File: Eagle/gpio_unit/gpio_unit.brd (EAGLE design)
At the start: 90.5 x 25.4 mm, 11 parts, among them X1 RASPI_GPIO_B+_PIN

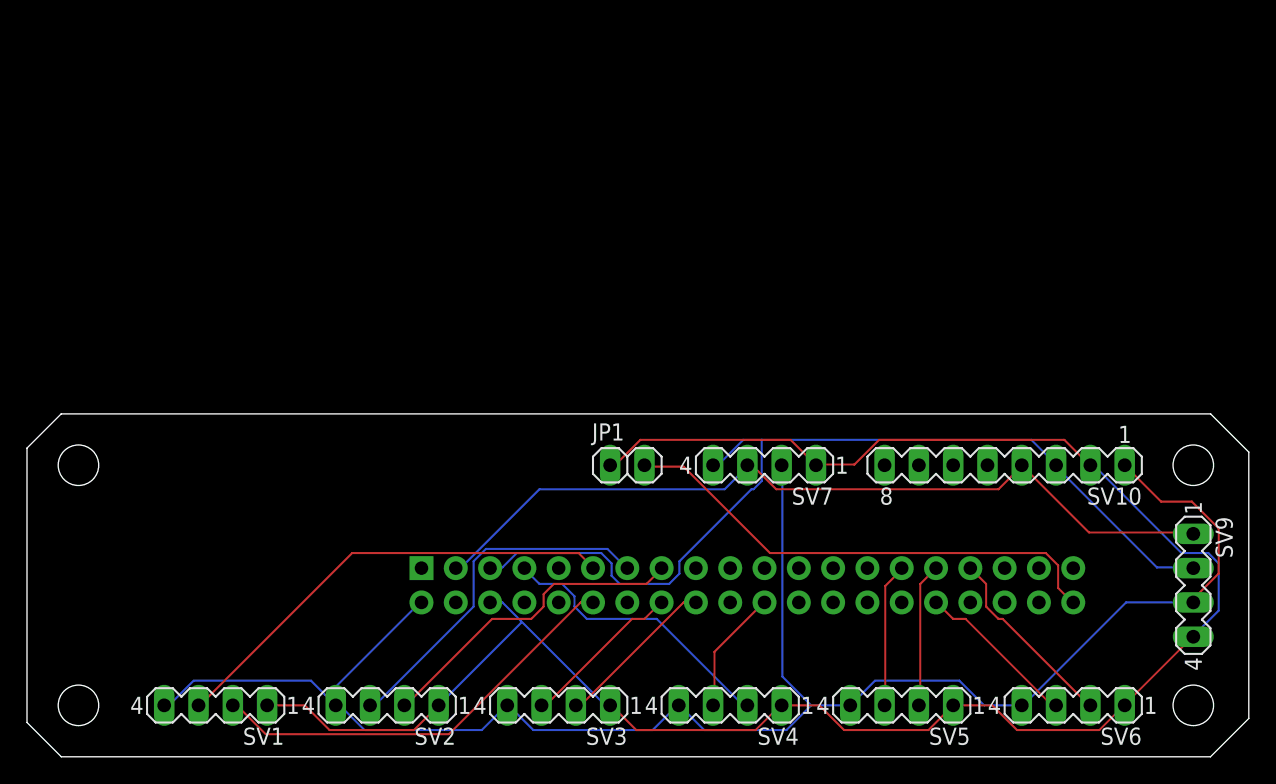
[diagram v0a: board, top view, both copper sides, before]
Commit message: RPi GPIO unit
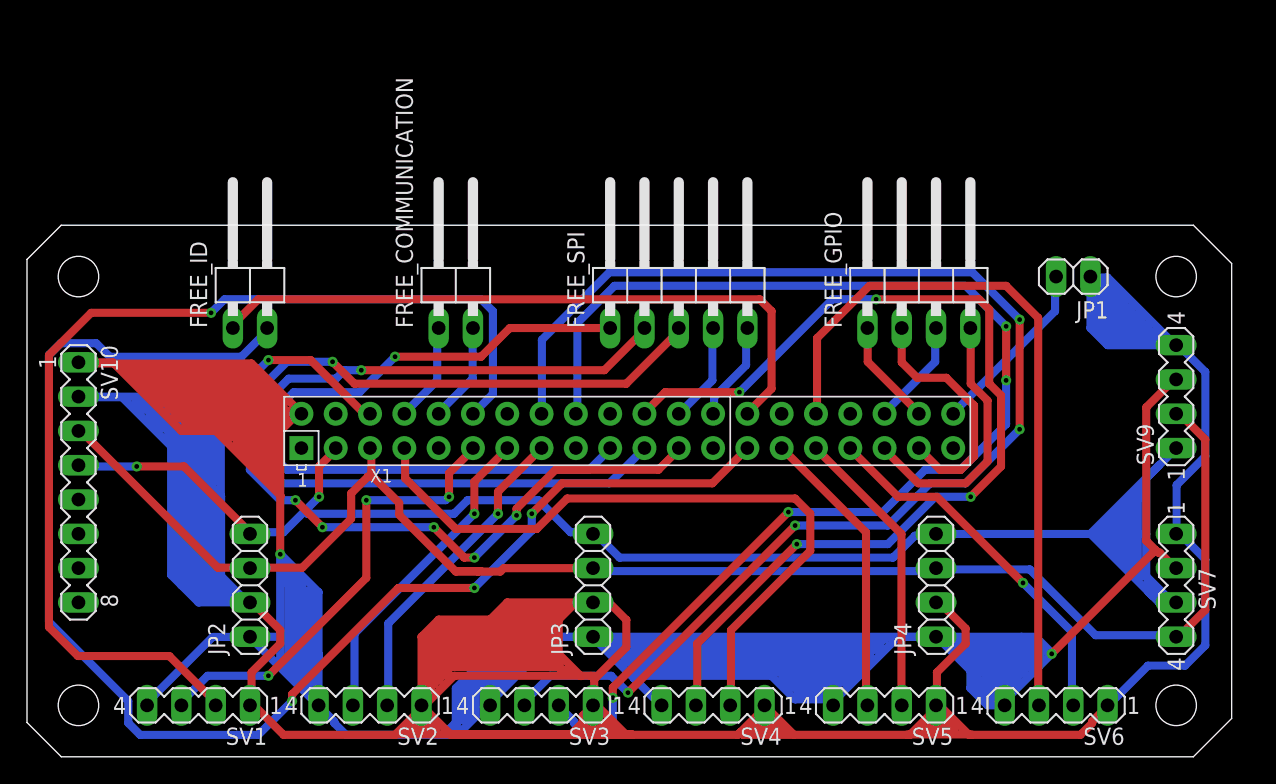
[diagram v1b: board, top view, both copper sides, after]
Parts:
- added FREE_COMMUNICATION, FREE_ID: (no value), pinhead:1X02/90
- added FREE_GPIO: (no value), pinhead:1X04/90
- added FREE_SPI: (no value), pinhead:1X05/90
- added JP2, JP3, JP4: (no value), pinhead:1X04
- moved SV10 68.6 mm to (3.81, 20.3), turned to 270 degrees
- moved JP1 35.9 mm to (77.5, 35.6), turned to 180 degrees
- moved SV7 31.8 mm to (85.1, 12.7), turned to 270 degrees
- moved X1 14.5 mm to (44.5, 24.1), flipped to the top, turned to 0 degrees
- moved SV9 14.0 mm to (85.1, 26.7), turned to 90 degrees
- moved SV2 1.27 mm to (25.4, 3.81)
- moved SV4 1.27 mm to (50.8, 3.81)
- moved SV1 1.27 mm to (12.7, 3.81)
- moved SV3 1.27 mm to (38.1, 3.81)
- moved SV5 1.27 mm to (63.5, 3.81)
- moved SV6 1.27 mm to (76.2, 3.81)
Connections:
- new net N$16: FREE_SPI.1, X1.19
- new net N$17: FREE_SPI.2, X1.21
- new net N$18: FREE_SPI.3, X1.23
- new net N$19: FREE_SPI.4, X1.24
- new net N$20: FREE_SPI.5, X1.26
- new net N$21: FREE_COMMUNICATION.1, X1.8
- new net N$22: FREE_COMMUNICATION.2, X1.10
- new net N$23: FREE_ID.1, X1.28
- new net N$24: FREE_ID.2, X1.27
- new net N$25: FREE_GPIO.4, X1.35
- new net N$26: FREE_GPIO.3, X1.36
- new net N$27: FREE_GPIO.2, X1.37
- new net N$28: FREE_GPIO.1, X1.38
- net N$1: now also JP2.2, JP3.2, JP4.2
- net N$15: now also JP2.4, JP3.4, JP4.4
- net N$5: now also JP2.3, JP3.3, JP4.3
- net VDD: now also JP2.1, JP3.1, JP4.1
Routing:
- net N$1: track 142.3 -> 298.4 mm, vias 0 -> 1
- net VDD: track 130.8 -> 243.6 mm, vias 0 -> 2
- net N$24: track 0.00 -> 103.7 mm, vias 0 -> 3
- net N$7: track 12.0 -> 98.8 mm, vias 0 -> 4
- net N$8: track 12.0 -> 93.4 mm, vias 0 -> 4
- net N$18: track 0.00 -> 78.8 mm, vias 0 -> 6
- net N$17: track 0.00 -> 64.9 mm, vias 0 -> 1
- net N$9: track 9.29 -> 73.9 mm, vias 0 -> 4
- net N$15: track 61.5 -> 120.0 mm, vias 0 -> 2
- net N$16: track 0.00 -> 56.4 mm, vias 0 -> 1
- net N$23: track 0.00 -> 49.6 mm
- net N$5: track 69.2 -> 118.0 mm
- net N$3: track 31.6 -> 78.2 mm, vias 0 -> 1
- net N$13: track 12.0 -> 53.3 mm
- net N$10: track 21.2 -> 51.8 mm
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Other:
- board size 90.5 x 25.4 mm -> 89.2 x 39.4 mm
- board text added: "FROM UPS"
- board text added: "GND"
- board text added: "GPIO04"
- board text added: "GPIO05"
- board text added: "GPIO06"
- board text added: "GPIO12"
- board text added: "GPIO13"
- board text added: "GPIO16"
- board text added: "GPIO17"
- board text added: "GPIO18"
- board text added: "GPIO19"
- board text added: "GPIO20"
- board text added: "GPIO22"
- board text added: "GPIO23"
- board text added: "GPIO24"
- board text added: "GPIO25"
- board text added: "GPIO26"
- board text added: "GPIO27"
- board text added: "ID_SC"
- board text added: "ID_SD"
- board text added: "RXD"
- board text added: "SCL"
- board text added: "SDA"
- board text added: "SPI_CE0"
- board text added: "SPI_CE1"
- board text added: "SPI_MISO"
- board text added: "SPI_MOSI"
- board text added: "SPI_SCLK"
- board text added: "TXD"
- board text added: "VDD"
